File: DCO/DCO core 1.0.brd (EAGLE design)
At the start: 35.5 x 17.8 mm, 23 parts, among them IC1 PIC16F18325SL, IC2 MAX5216, IC4 TL072D

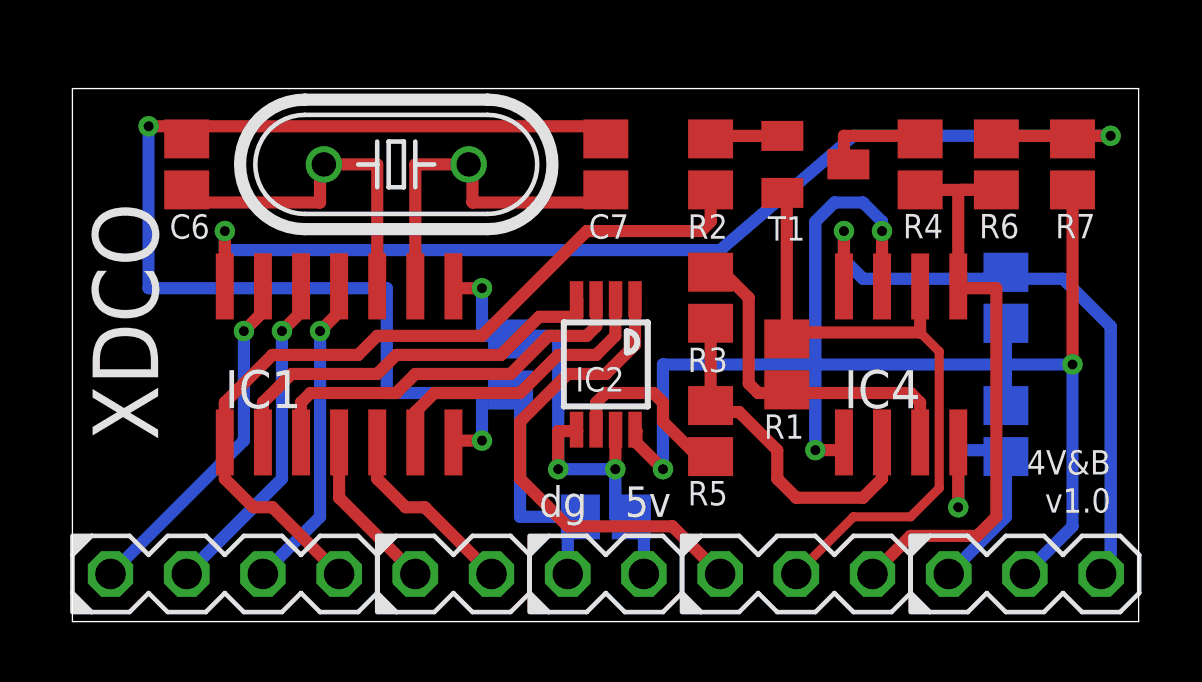
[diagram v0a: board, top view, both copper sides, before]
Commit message: Larger pin pads
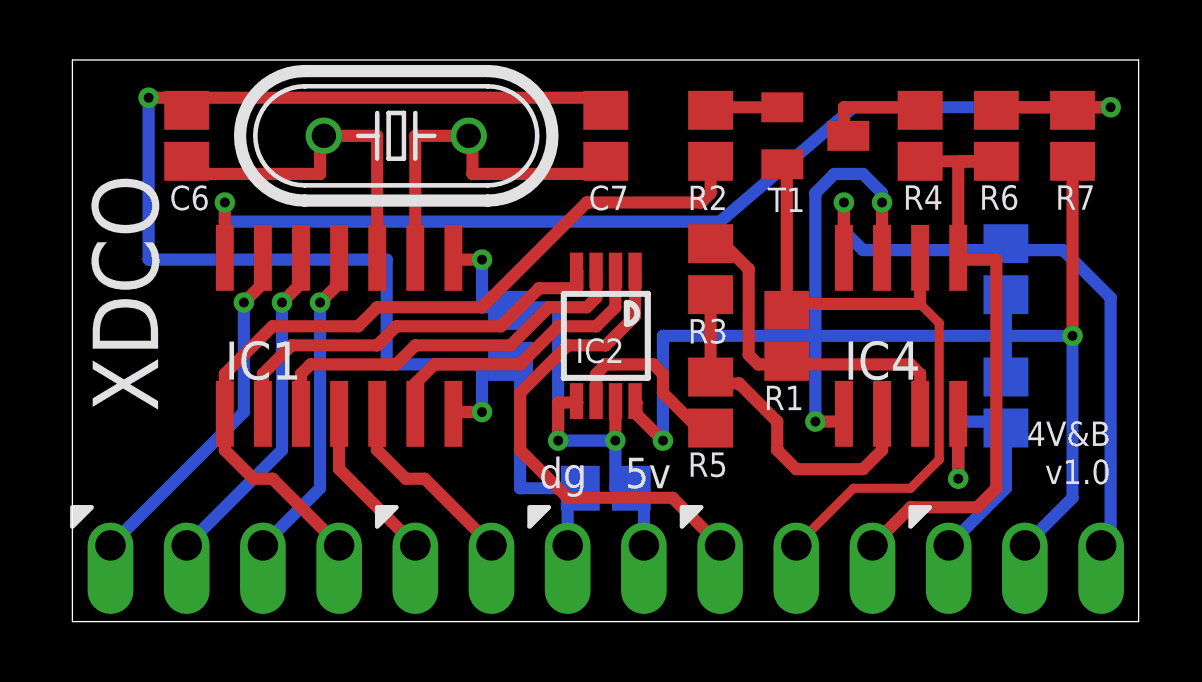
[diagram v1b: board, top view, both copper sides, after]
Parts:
- APWR, CORE: device joakim:MA03-1J -> joakim:SIP-PIN03-1J
- COM: device joakim:MA04-1J -> joakim:SIP-PIN04-1J
- DPWR, SYNC: value (none) -> MA02-1JP; device joakim:MA02-1J -> joakim:SIP-PIN02-1J
- moved SYNC 1.59 mm to (12.7, 2.54)
- moved DPWR 1.59 mm to (17.8, 2.54)
- moved C2 0.95 mm to (31.1, 7.30)
- moved C3 0.95 mm to (31.1, 11.7)
- moved C5 0.95 mm to (14.6, 9.53)
- moved IC1 0.95 mm to (8.89, 9.53)
- moved IC2 0.95 mm to (17.8, 9.53)
- moved IC4 0.95 mm to (27.6, 9.53)
- moved R1 0.95 mm to (23.8, 9.53)
- moved R3 0.95 mm to (21.3, 11.7)
- moved R5 0.95 mm to (21.3, 7.30)
- moved APWR 0.95 mm to (31.8, 2.54)
- moved C1 0.95 mm to (17.8, 4.45)
- moved COM 0.95 mm to (5.08, 2.54)
- moved CORE 0.95 mm to (24.1, 2.54)
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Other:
- board size 35.5 x 17.8 mm -> 35.5 x 18.7 mm
